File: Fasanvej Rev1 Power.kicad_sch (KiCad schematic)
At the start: 58 parts

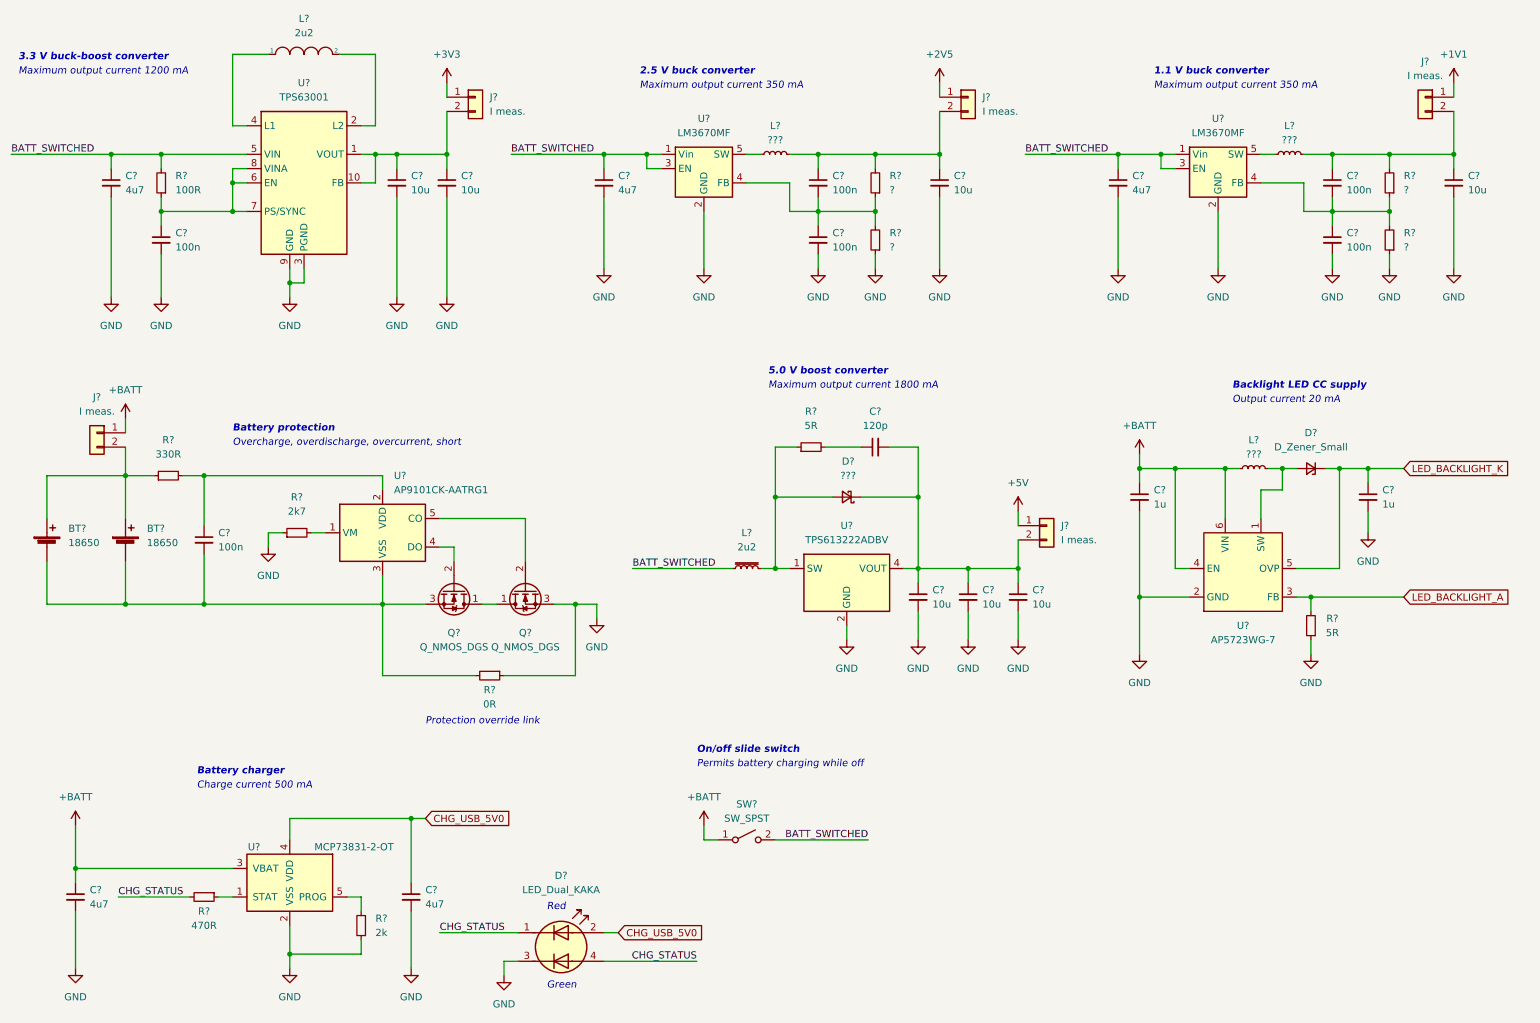
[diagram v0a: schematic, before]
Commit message: Finalized schematics some more. Still missing a few footprints.
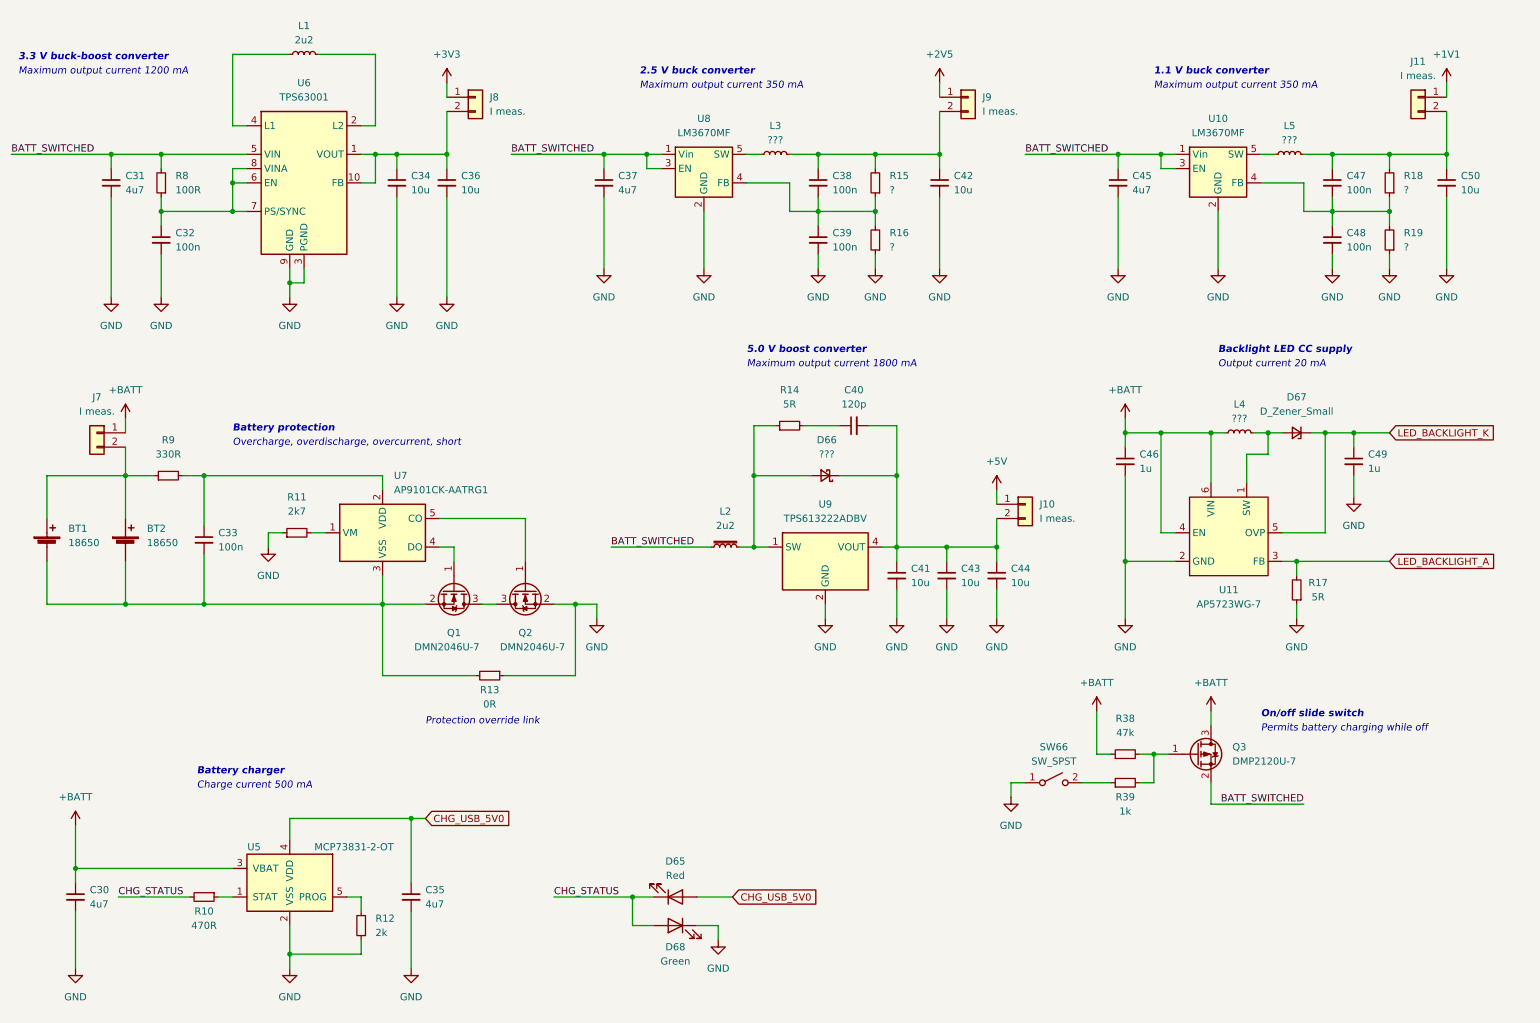
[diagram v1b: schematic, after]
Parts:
- removed D?: LED_Dual_KAKA, symbol Device:LED_Dual_KAKA
- removed L?: 2u2, symbol pspice:INDUCTOR
- added D65: Red, LED_SMD:LED_0805_2012Metric_Pad1.15x1.40mm_HandSolder, symbol Device:LED
- added D68: Green, LED_SMD:LED_0805_2012Metric_Pad1.15x1.40mm_HandSolder, symbol Device:LED
- added L1: 2u2, symbol Device:L_Small
- added Q3: DMP2120U-7, Package_TO_SOT_SMD:SOT-23_Handsoldering, symbol Device:Q_PMOS_GSD
- added R38: 47k, Resistor_SMD:R_0603_1608Metric_Pad0.98x0.95mm_HandSolder, symbol Device:R_Small
- added R39: 1k, Resistor_SMD:R_0603_1608Metric_Pad0.98x0.95mm_HandSolder, symbol Device:R_Small
- Q1, Q2: renamed from Q?; value Q_NMOS_DGS -> DMN2046U-7; footprint (none) -> Package_TO_SOT_SMD:SOT-23_Handsoldering; symbol Device:Q_NMOS_DGS -> Device:Q_NMOS_GSD
- R9: renamed from R?; footprint Resistor_SMD:R_0603_1608Metric_Pad0.98x0.95mm_HandSolder -> Resistor_SMD:R_1206_3216Metric_Pad1.30x1.75mm_HandSolder
- SW66: renamed from SW?; footprint (none) -> Button_Switch_THT:SW_CuK_JS202011AQN_DPDT_Angled
- gave numbers to parts that had none: 52
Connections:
- net +BATT: now also Q3.3 (D), R38.1; no longer SW66.1 (A)
- net BATT_SWITCHED: now also Q3.2 (S); no longer SW66.2 (B)
- net CHG_STATUS: now also D65.1 (K), D68.2 (A)
- net CHG_USB_5V0: now also D65.2 (A)
- net GND: now also Q2.2 (S), SW66.1 (A), D68.1 (K); no longer Q2.3 (S)
- net at BT1.2 (-), BT2.2 (-), C33.2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: now also Q1.2 (S); no longer Q1.3 (S)
- net at U7.4 (DO): now also Q1.1 (G); no longer Q1.2 (G)
- net at U7.5 (CO): now also Q2.1 (G); no longer Q2.2 (G)
- net at U6.4 (L1): now also L1.1
- net at U6.2 (L2): now also L1.2
- new net: Q3.1 (G), R38.2, R39.2
- new net: R39.1, SW66.2 (B)
- new net: Q1.3 (D), Q2.3 (D)
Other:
- note removed: "Green"
- note removed: "Red"
- moved on the sheet: C40, C41, C43, C44, C46, C49, C50, D66, D67, J10, J11, L2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

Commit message: Schematic finalized. Started PCB layout.
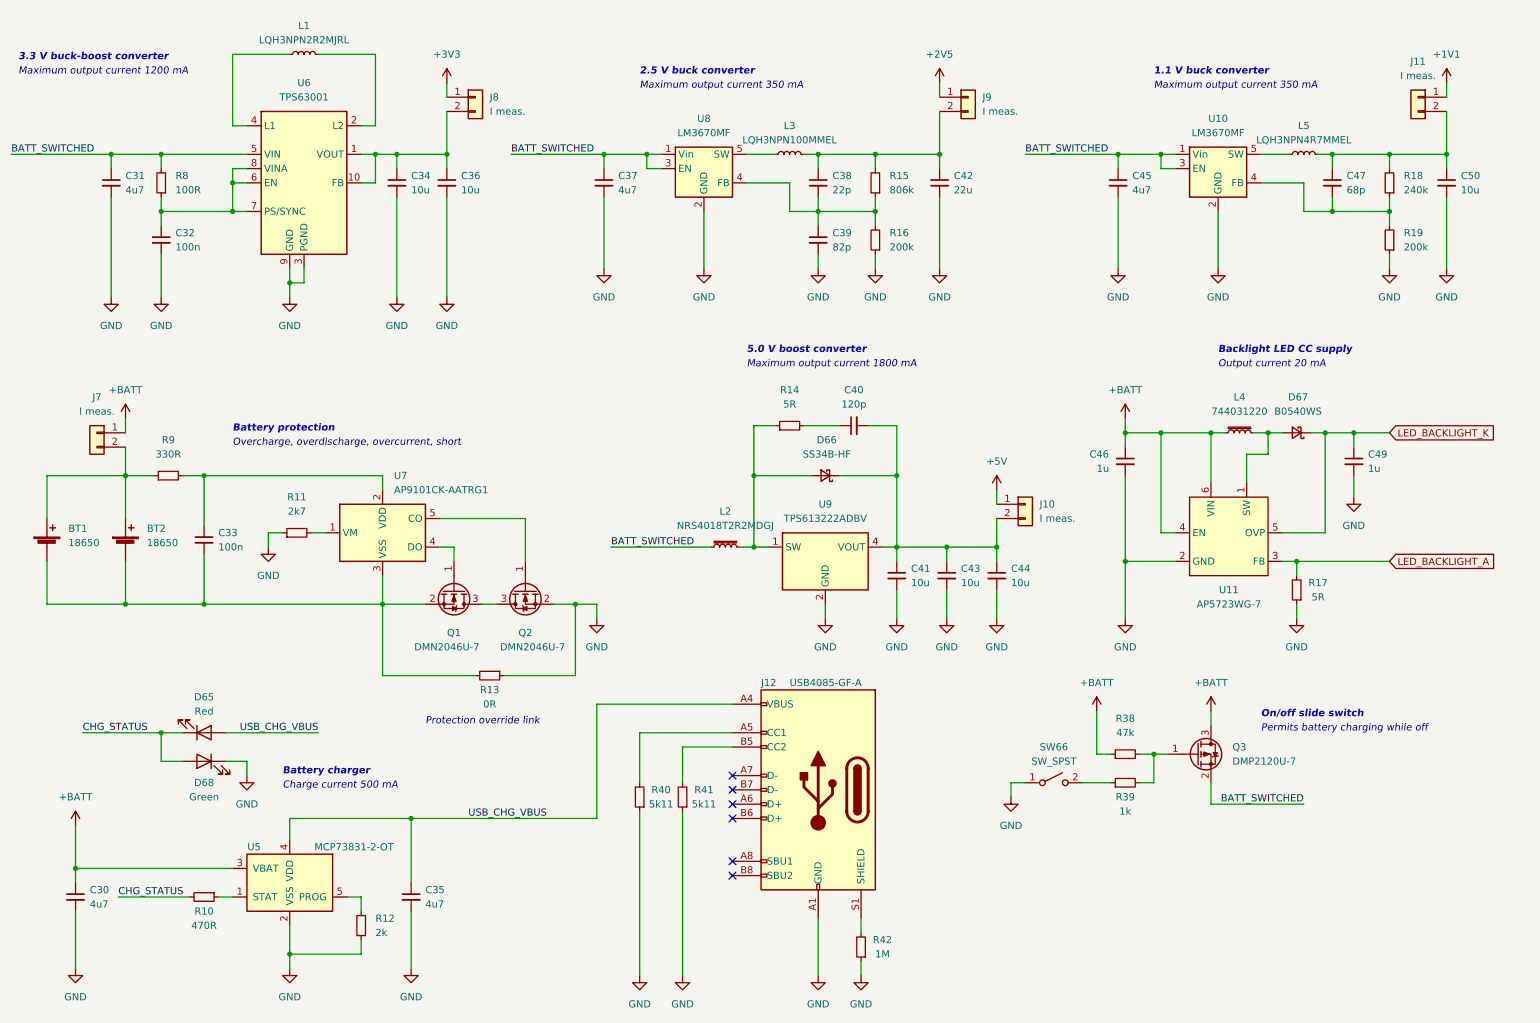
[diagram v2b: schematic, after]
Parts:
- removed C48: 100n, Capacitor_SMD:C_0603_1608Metric_Pad1.08x0.95mm_HandSolder, symbol Device:C_Small
- removed D67: D_Zener_Small, symbol Device:D_Zener_Small
- removed L4: ???, symbol Device:L_Small
- added D67: B0540WS, Diode_SMD:D_SOD-323_HandSoldering, symbol Device:D_Schottky_Small
- added J12: USB4085-GF-A, Connector_USB:USB_C_Receptacle_GCT_USB4085, symbol Connector:USB_C_Receptacle_USB2.0
- added L4: 744031220, Inductor_SMD:L_Wuerth_WE-TPC-3816, symbol Device:L_Iron_Small
- added R40, R41: 5k11, Resistor_SMD:R_0603_1608Metric_Pad0.98x0.95mm_HandSolder, symbol Device:R_Small
- added R42: 1M, Resistor_SMD:R_0603_1608Metric_Pad0.98x0.95mm_HandSolder, symbol Device:R_Small
- C38: value 100n -> 22p
- C39: value 100n -> 82p
- C42: value 10u -> 22u; footprint Capacitor_SMD:C_1206_3216Metric_Pad1.33x1.80mm_HandSolder -> Capacitor_SMD:C_1210_3225Metric_Pad1.33x2.70mm_HandSolder
- C47: value 100n -> 68p
- D66: value ??? -> SS34B-HF; footprint (none) -> Diode_SMD:D_SMB_Handsoldering
- L1: value 2u2 -> LQH3NPN2R2MJRL; footprint (none) -> RISRES Library:L_SMD_3030
- L2: value 2u2 -> NRS4018T2R2MDGJ; footprint (none) -> Inductor_SMD:L_Taiyo-Yuden_NR-40xx_HandSoldering
- L3: value ??? -> LQH3NPN100MMEL; footprint (none) -> RISRES Library:L_SMD_3030
- L5: value ??? -> LQH3NPN4R7MMEL; footprint (none) -> RISRES Library:L_SMD_3030
- R15: value ? -> 806k
- R16, R19: value ? -> 200k
- R18: value ? -> 240k
- U11: footprint (none) -> Package_TO_SOT_SMD:SOT-23-6_Handsoldering
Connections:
- net +BATT: now also L4.1
- net GND: now also J12.A1 (GND), J12.A12 (GND), J12.B1 (GND), J12.B12 (GND), R40.1, R41.1, R42.1
- net LED_BACKLIGHT_K: now also D67.1 (K)
- net at U11.1 (SW): now also D67.2 (A), L4.2
- net CHG_USB_5V0 renamed USB_CHG_VBUS
- net USB_CHG_VBUS: now also J12.A4 (VBUS), J12.A9 (VBUS), J12.B4 (VBUS), J12.B9 (VBUS)
- new net: J12.S1 (SHIELD), R42.2
- new net: J12.A5 (CC1), R40.2
- new net: J12.B5 (CC2), R41.2
- no-connect marks 0 -> 6
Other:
- moved on the sheet: D65, D68, L3

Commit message: Made a lot of progress laying out PCB
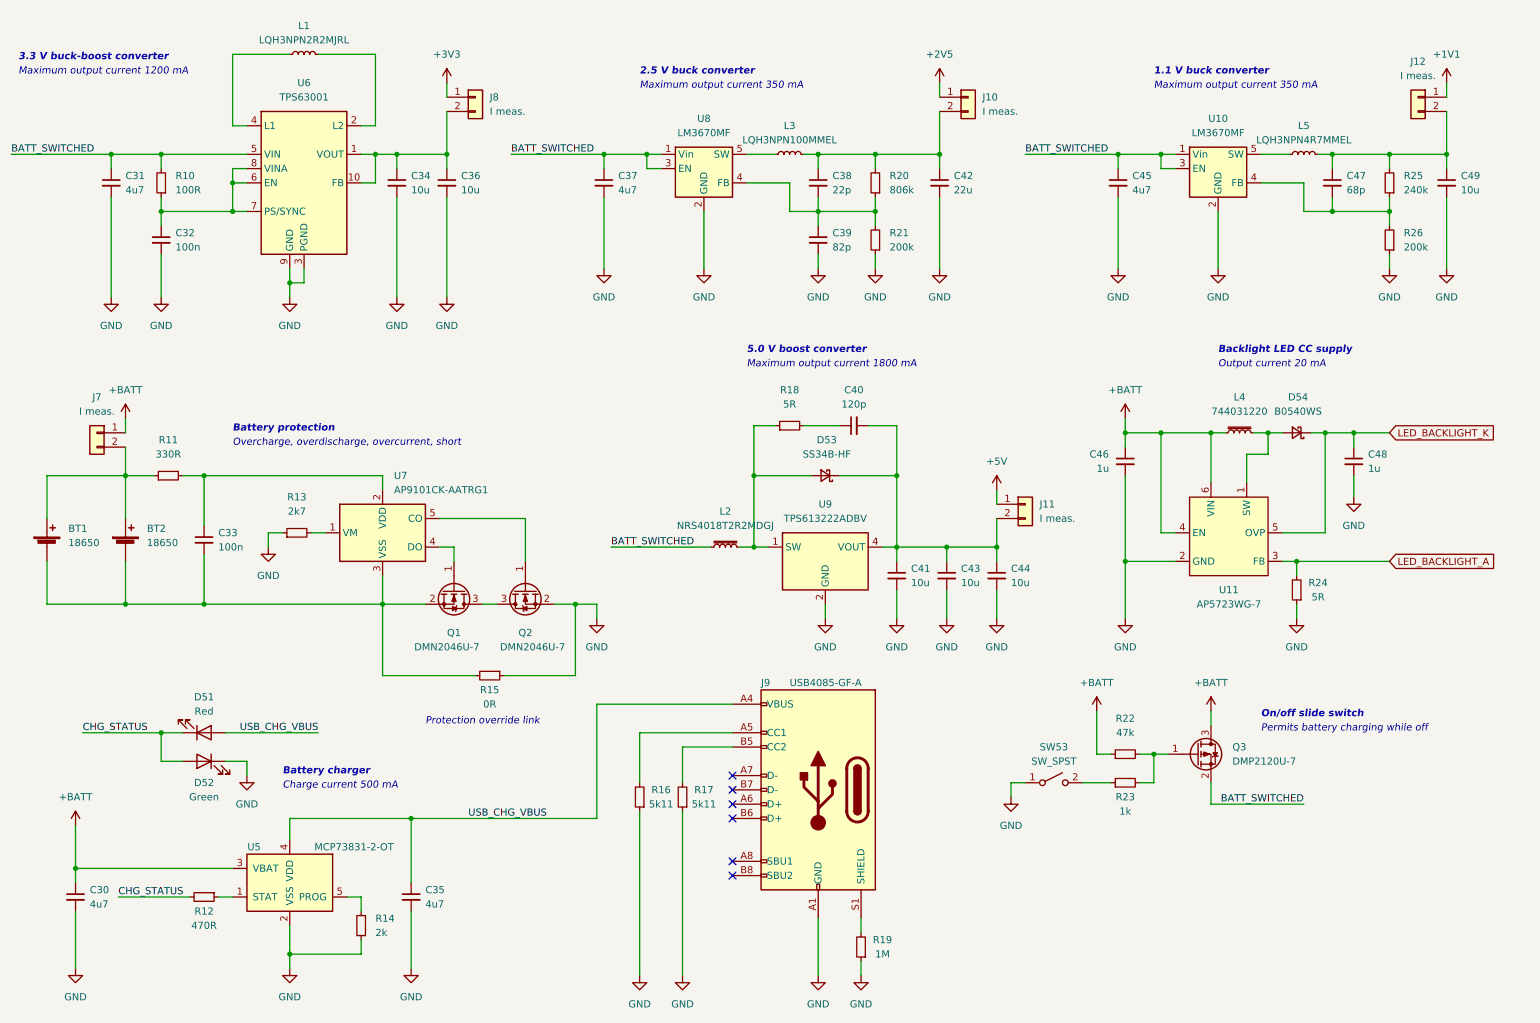
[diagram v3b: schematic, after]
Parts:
- renumbered C49 to C48, C50 to C49, D65 to D51, D68 to D52, D66 to D53, D67 to D54, J9 to J10, J10 to J11, J11 to J12, J12 to J9, R8 to R10, R9 to R11, R10 to R12, R11 to R13, R12 to R14, R13 to R15, R40 to R16, R41 to R17, R14 to R18, R42 to R19, R15 to R20, R16 to R21, R38 to R22, R39 to R23, R17 to R24, R18 to R25, R19 to R26, SW66 to SW53
